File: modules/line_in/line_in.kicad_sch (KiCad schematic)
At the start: 30 parts, among them J1 AudioJack3, U1 TL072, U2 TL072, U3 TL072

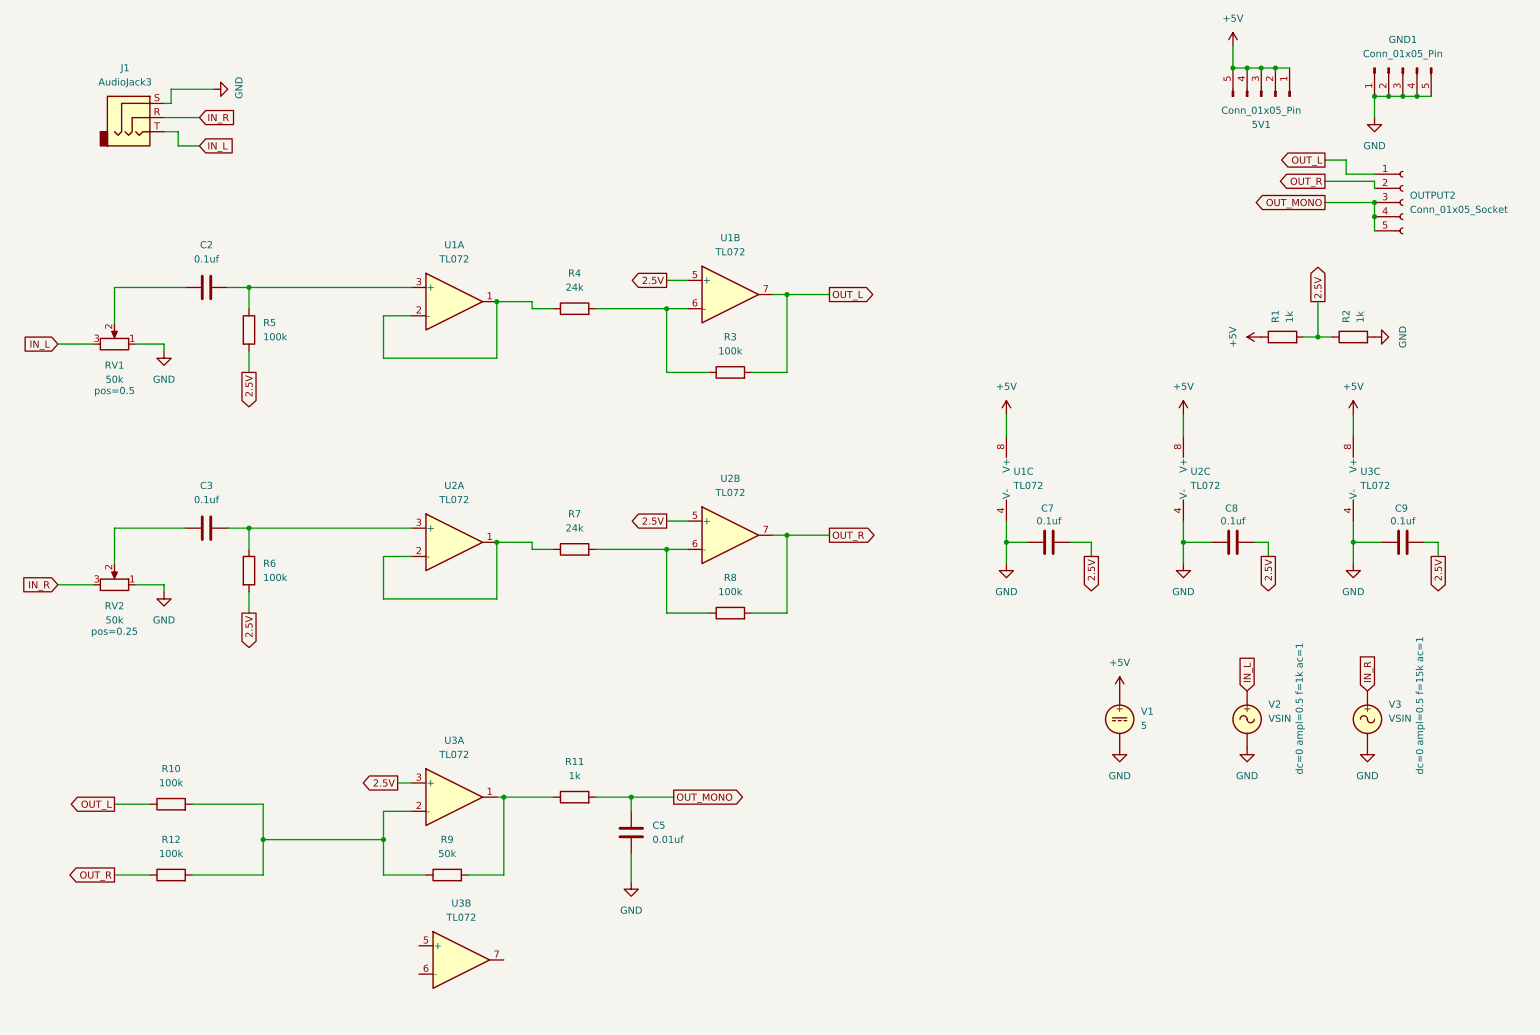
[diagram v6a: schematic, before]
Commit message: Finished building the line_in module.
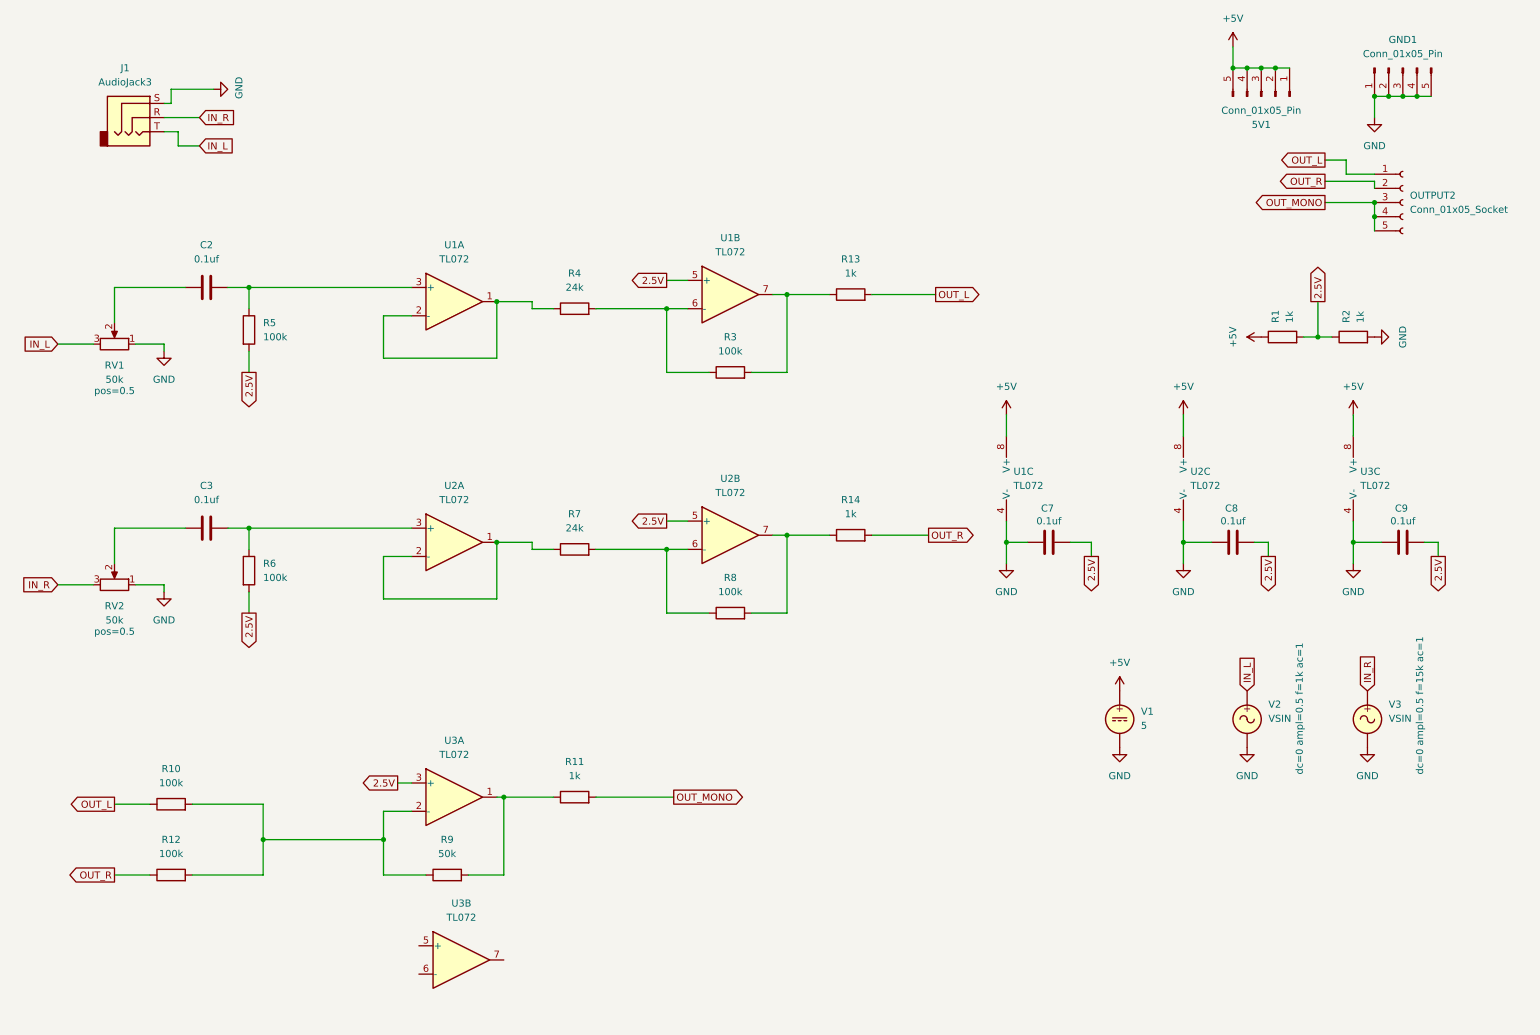
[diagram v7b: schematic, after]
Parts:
- removed C5: 0.01uf, symbol Device:C
- added R13, R14: 1k, Resistor_SMD:R_0402_1005Metric, symbol Device:R
- C2, C3, C7, C8, C9: footprint (none) -> Capacitor_SMD:C_0402_1005Metric
- R1, R10, R11, R12, R2, R3, R4, R5, R6, R7, R8, R9: footprint (none) -> Resistor_SMD:R_0402_1005Metric
- RV1, RV2: footprint (none) -> BreadModular_Pots:Potentiometer_RV09
- U1, U2, U3: footprint (none) -> Package_SO:SOIC-8-1EP_3.9x4.9mm_P1.27mm_EP2.29x3mm
- V1, V2, V3: now left out of the parts list
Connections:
- net OUT_L: now also R13.2; no longer R3.2, U1.7
- net OUT_R: now also R14.2; no longer R8.2, U2.7
- new net: R13.1, R3.2, U1.7
- new net: R14.1, R8.2, U2.7

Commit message: Update line_in to use MCP6001 and 3V3.
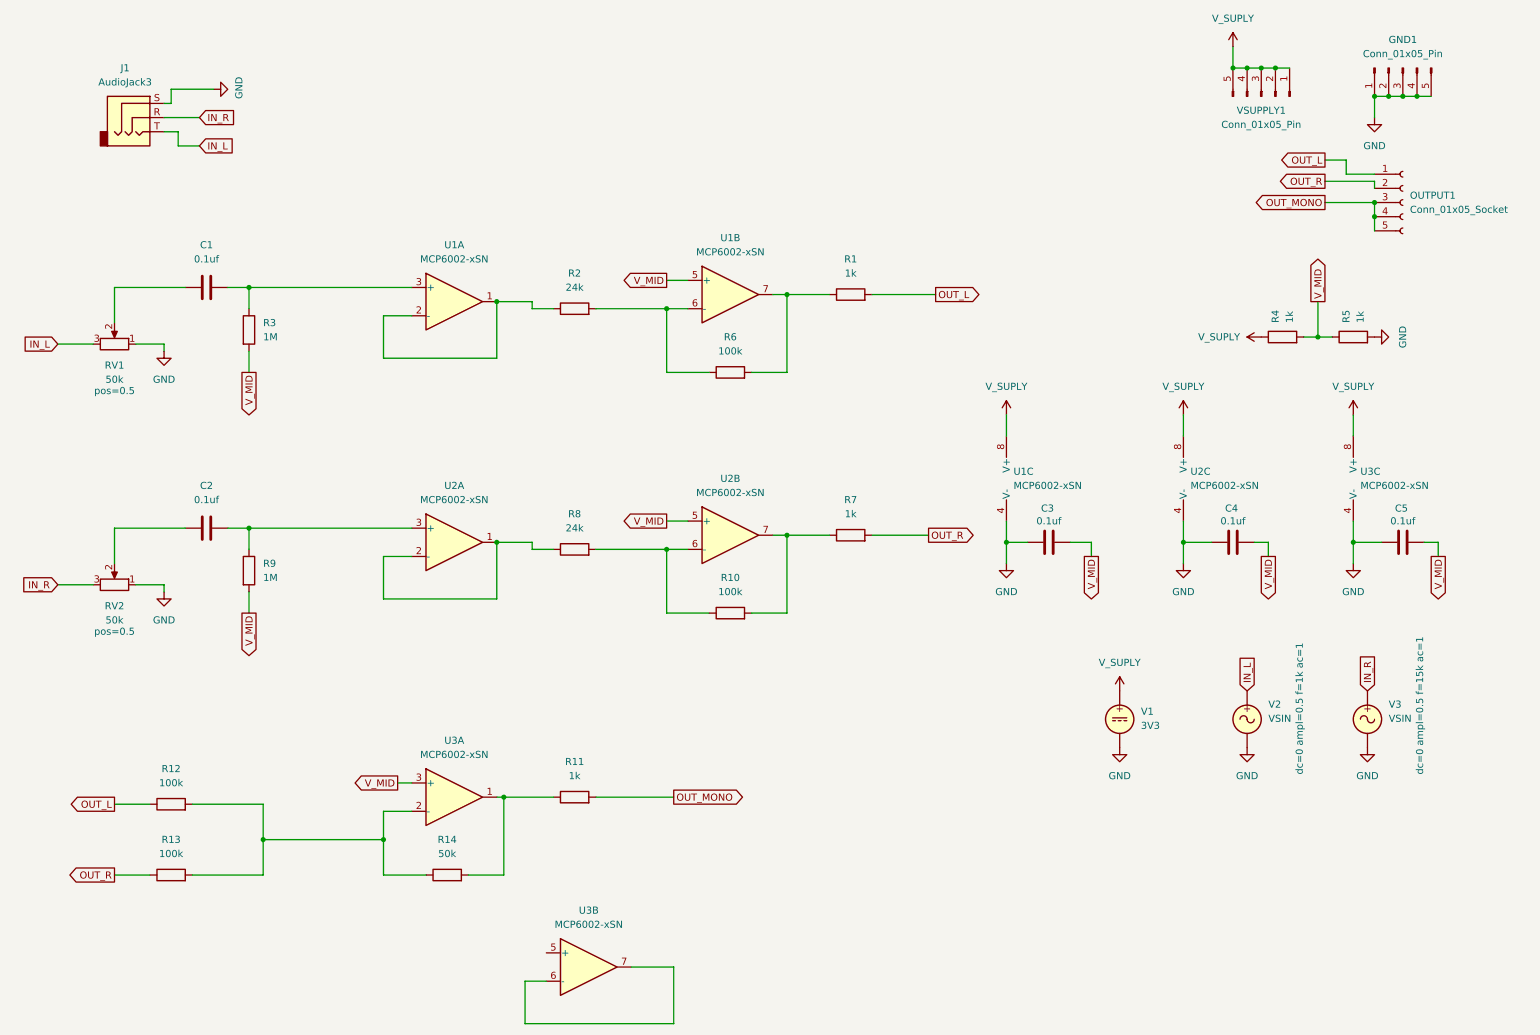
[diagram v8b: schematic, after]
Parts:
- removed U1, U2, U3: TL072, Package_SO:SOIC-8-1EP_3.9x4.9mm_P1.27mm_EP2.29x3mm, symbol Amplifier_Operational:TL072
- added U1, U2, U3: MCP6002-xSN, Package_SO:SOIC-8-1EP_3.9x4.9mm_P1.27mm_EP2.29x3mm, symbol Amplifier_Operational:MCP6002-xSN
- GND1: footprint Connector_PinHeader_2.54mm:PinHeader_1x05_P2.54mm_Vertical -> BreadModular_MISC:Power_Connector
- R3: renamed from R5; value 100k -> 1M
- R9: renamed from R6; value 100k -> 1M
- V1: value 5 -> 3V3; now in the parts list
- V2, V3: now in the parts list
- VSUPPLY1: renamed from 5V1; footprint Connector_PinHeader_2.54mm:PinHeader_1x05_P2.54mm_Vertical -> BreadModular_MISC:Power_Connector
- renumbered C2 to C1, C3 to C2, C7 to C3, C8 to C4, C9 to C5, OUTPUT2 to OUTPUT1, R13 to R1, R8 to R10, R10 to R12, R12 to R13, R9 to R14, R4 to R2, R1 to R4, R2 to R5, R3 to R6, R14 to R7, R7 to R8
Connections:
- net GND: now also U1.4 (V-), U2.4 (V-), U3.4 (V-)
- net at R12.2, R13.2, R14.1: now also U3.2 (-)
- net at R11.1, R14.2: now also U3.1
- net at C2.2, R9.1: now also U2.3 (+)
- net at R1.1, R6.2: now also U1.7
- net at R8.1: now also U2.1, U2.2 (-)
- net at R10.2, R7.1: now also U2.7
- net at R2.2, R6.1: now also U1.6 (-)
- net at C1.2, R3.1: now also U1.3 (+)
- net at R10.1, R8.2: now also U2.6 (-)
- net at R2.1: now also U1.1, U1.2 (-)
- net +5V renamed V_SUPLY
- net V_SUPLY: now also U1.8 (V+), U2.8 (V+), U3.8 (V+)
- net 2.5V renamed V_MID
- net V_MID: now also U1.5 (+), U2.5 (+), U3.3 (+)
- new net: U3.6 (-), U3.7
